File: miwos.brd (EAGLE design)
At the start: 115 x 115 mm, 47 parts

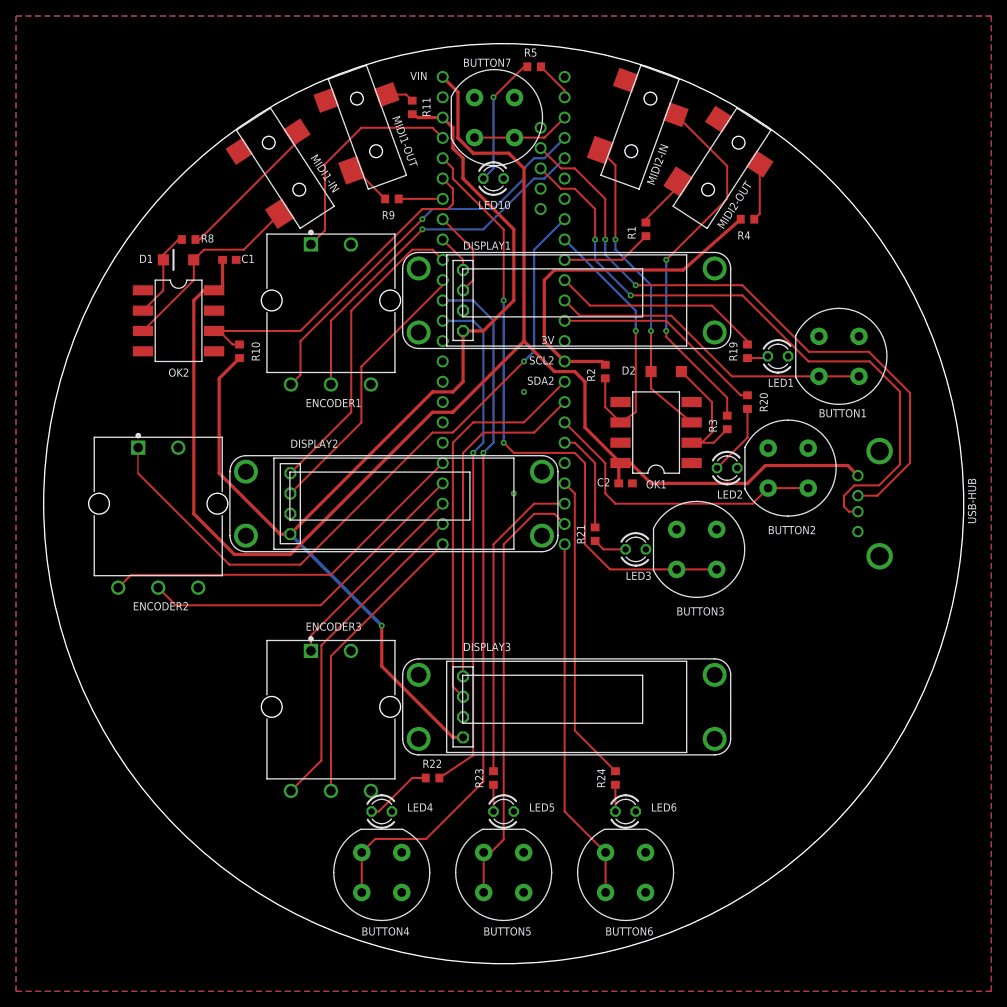
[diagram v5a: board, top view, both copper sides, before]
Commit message: Various changes, add mounting holes
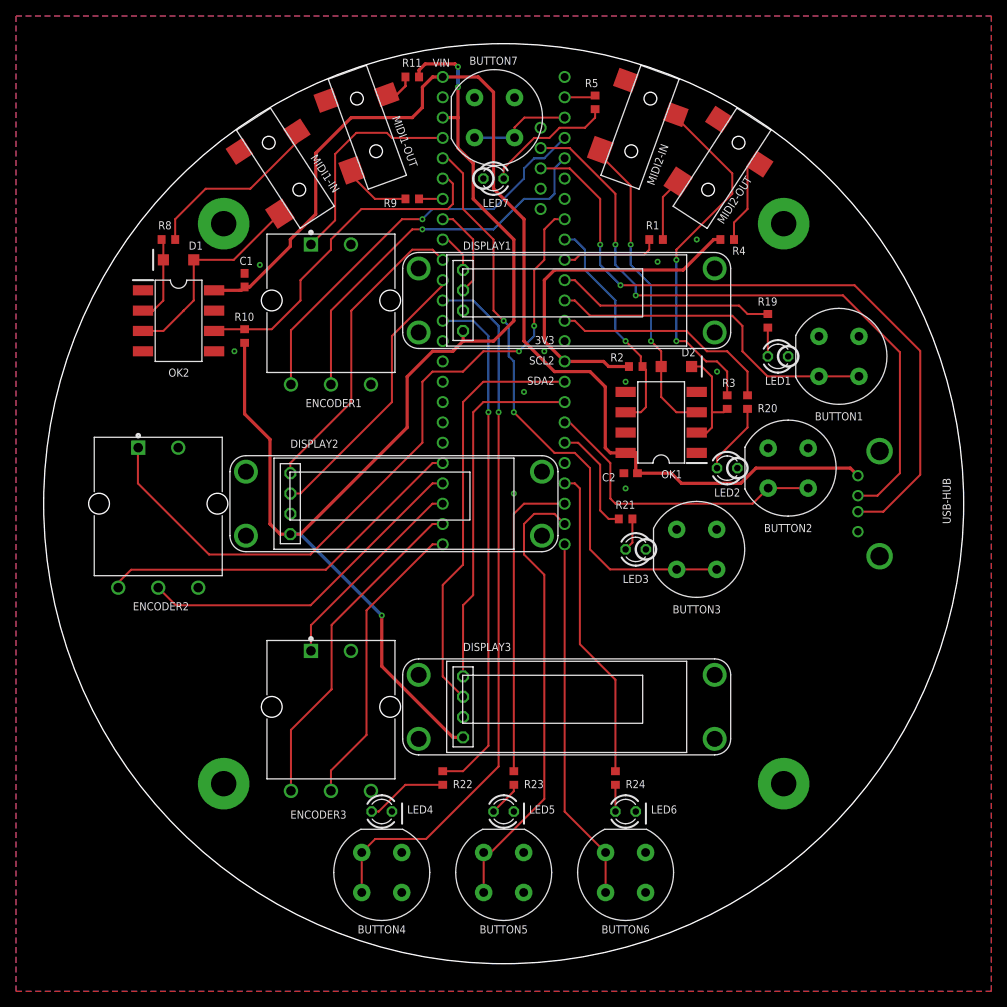
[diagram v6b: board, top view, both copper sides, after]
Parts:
- added P1, P2, P3, P4: MOUNT_CH, sol_pin:MOUNT_CH32
- moved R5 8.82 mm to (11.4, 50.2), turned to 270 degrees
- moved R19 4.58 mm to (33.0, 22.9)
- moved R21 4.26 mm to (15.2, -1.91), turned to 0 degrees
- moved R2 3.86 mm to (16.5, 17.1), turned to 0 degrees
- moved R11 3.81 mm to (-11.4, 53.3), turned to 0 degrees
- moved R4 3.59 mm to (27.9, 33.0)
- moved C1 3.18 mm to (-32.4, 27.9), turned to 90 degrees
- moved R9 2.54 mm to (-11.4, 38.1)
- moved R23 2.54 mm to (1.27, -34.3)
- moved R3 2.54 mm to (27.9, 12.7)
- moved R8 2.54 mm to (-41.9, 33.0)
- moved R10 2.01 mm to (-32.4, 21.0)
- moved R1 1.80 mm to (19.1, 33.0), turned to 180 degrees
- moved C2 1.42 mm to (15.9, 3.81), turned to 180 degrees
- moved D2 1.42 mm to (21.6, 17.1)
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- renumbered LED10 to LED7
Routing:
- net +5V: track 185.0 -> 142.2 mm
- net +3V3: track 180.7 -> 193.3 mm, vias 1 -> 3
- net N$3: track 81.3 -> 86.9 mm
- net RX2: track 33.9 -> 28.7 mm
- net N$21: track 7.17 -> 11.5 mm
- net N$10: track 19.0 -> 23.0 mm
- net ENCODER2-PUSH: track 86.6 -> 90.4 mm, vias 1 -> 2
- net N$16: track 17.4 -> 13.7 mm
- net SCL2: track 49.4 -> 52.7 mm
- net N$2: track 79.9 -> 83.0 mm
- net N$11: track 5.65 -> 8.58 mm
- net BUTTON3: track 77.9 -> 75.3 mm
- net ENCODER1-B: track 45.6 -> 48.2 mm
- net TX5: track 5.50 -> 2.96 mm
- net SDA2: track 43.3 -> 45.5 mm
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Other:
- board text added: "3V3"
- board text removed: "3V"

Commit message: Rotate LEDs
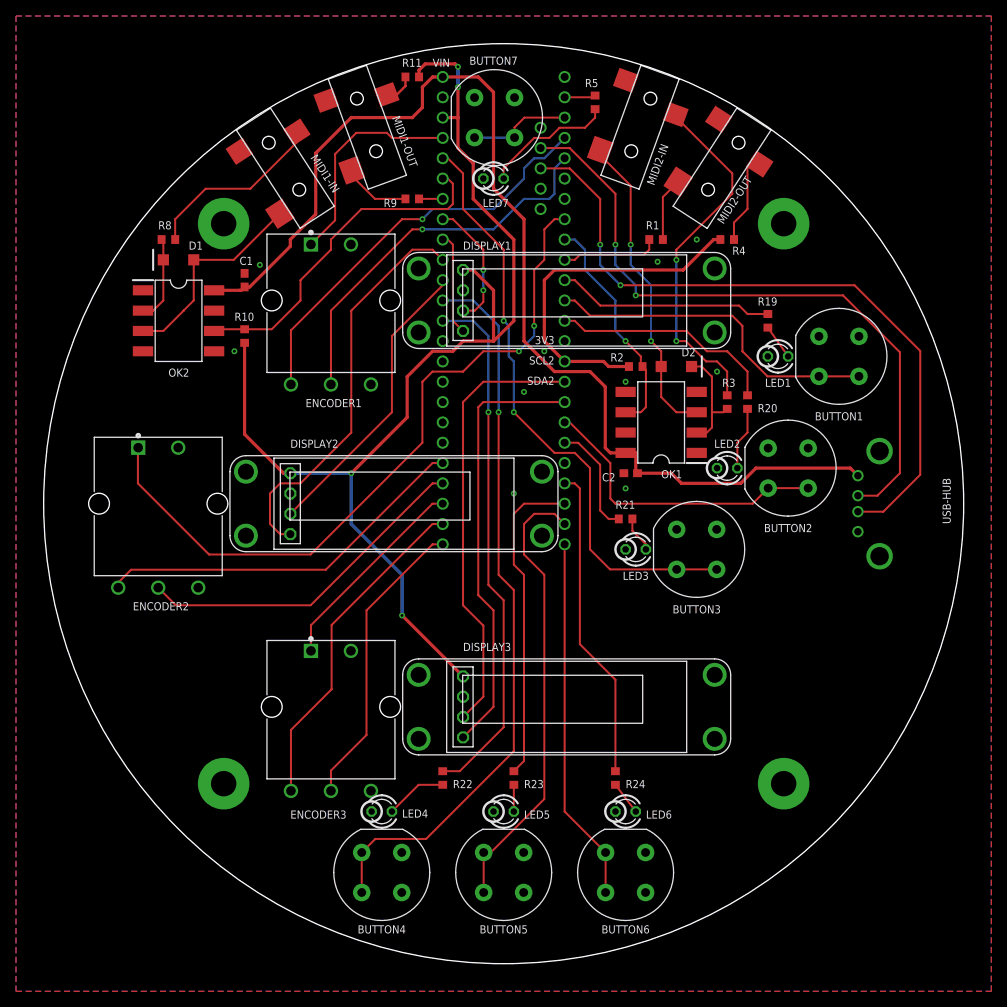
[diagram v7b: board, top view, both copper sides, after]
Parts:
- turned LED1 to 180 degrees
- turned LED2 to 180 degrees
- turned LED3 to 180 degrees
- turned LED4 to 180 degrees
- turned LED5 to 180 degrees
- turned LED6 to 180 degrees
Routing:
- net SDA1: track 38.6 -> 50.5 mm
- net SDA2: track 45.5 -> 54.7 mm
- net SDA: track 5.24 -> 12.9 mm
- net +3V3: track 193.3 -> 186.8 mm, vias 3 -> 4
- net SCL: track 11.7 -> 16.2 mm, vias 0 -> 2
- net N$31: track 10.3 -> 7.73 mm
- net SCL2: track 52.7 -> 55.2 mm
- net SCL1: track 35.3 -> 37.1 mm
- net BUTTON4: track 89.9 -> 91.5 mm
- net BUTTON4-LED: track 64.8 -> 66.1 mm
- net N$33: track 4.39 -> 3.34 mm
- net N$27: track 8.98 -> 7.93 mm
- net BUTTON5-LED: track 39.0 -> 40.1 mm
- net N$35: track 3.34 -> 4.20 mm
- net N$25: track 3.60 -> 4.40 mm
